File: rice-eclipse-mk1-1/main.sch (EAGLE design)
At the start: 199 parts, among them IC1 LMV321LICTRT, IC10 MCP6N11R, IC11 MCP6N11R, IC12 MCP6N11R, IC13 LMV321LICTRT, IC14 LMV321LICTRT, IC15 LMV321LICTRT, IC16 LMV321LICTRT, IC17 LMV321LICTRT, IC2 LMV321LICTRT, IC3 LMV321LICTRT, IC4 LMV321LICTRT, IC5 MCP6N11R, IC6 LMV321LICTRT, IC7 LMV321LICTRT, IC8 LMV321LICTRT, IC9 LMV321LICTRT, U6 1101M2S3CQE2

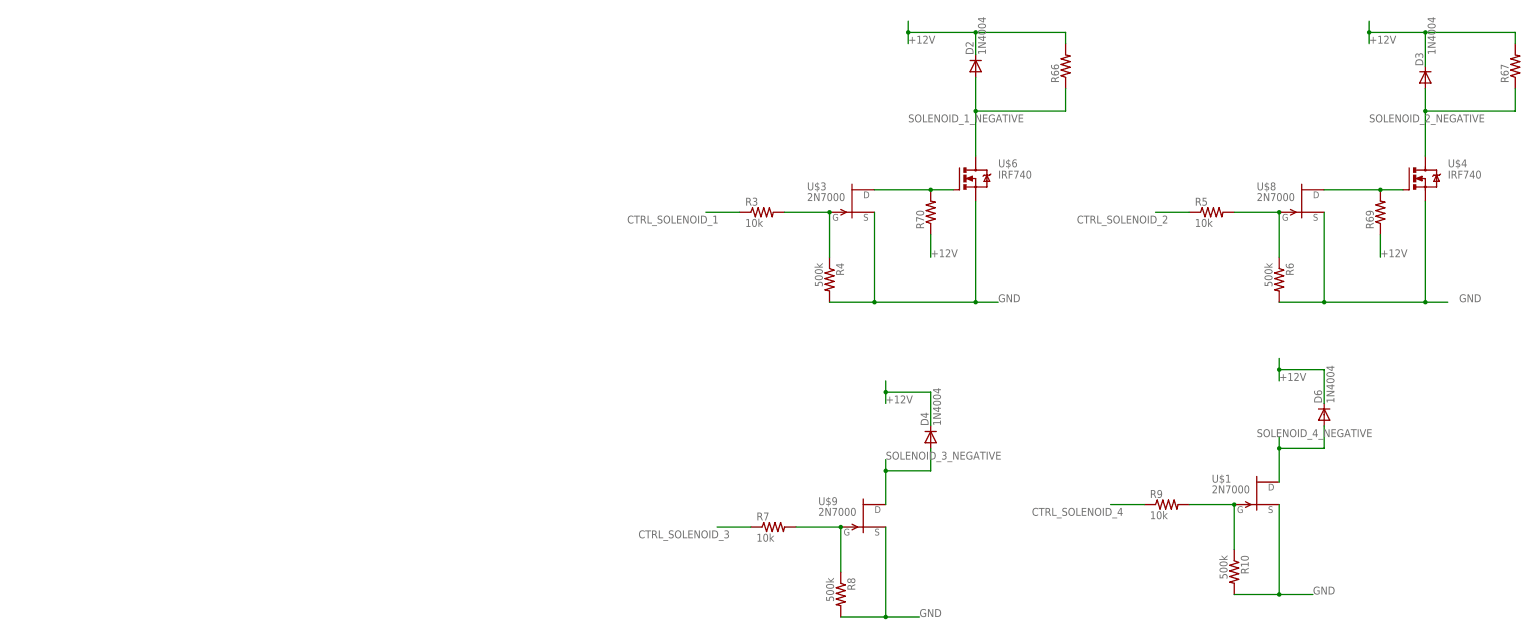
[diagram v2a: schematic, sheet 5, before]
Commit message: Add mosfet driver circuit
Currently have a version with a switch for using either
the 2N7000 or IRF740 (high current). Might be useful to
have a high current option for all the outputs since
propulsion seems to like adding more high-current valves.
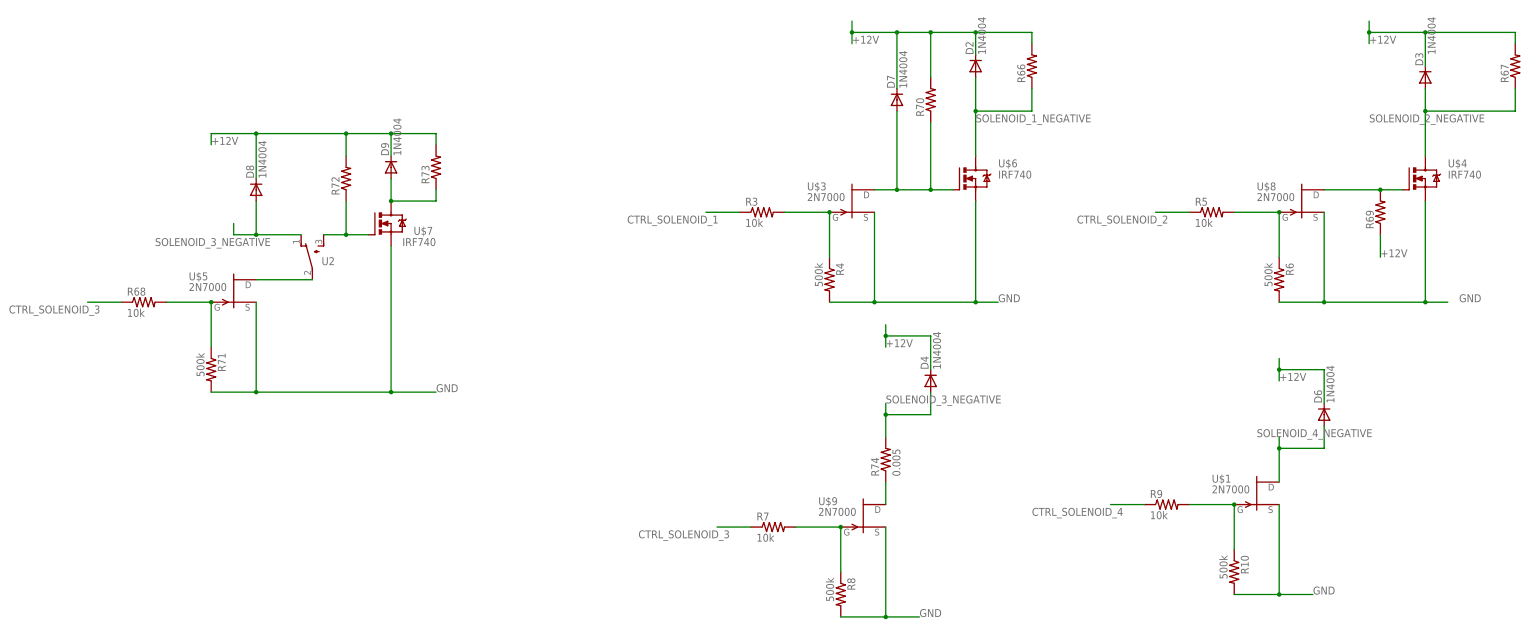
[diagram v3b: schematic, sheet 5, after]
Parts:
- added D7, D8, D9: 1N4004, diode:1N4004
- added R68: 10k, rcl:R-US_R0805
- added R71: 500k, rcl:R-US_R0805
- added R72, R73: (no value), rcl:R-US_R0805
- added R74: 0.005, rcl:R-US_R0805
- added U$5: 2N7000, transistor-fet-extra:2N7000
- added U$7: IRF740, transistor-power:IRF740
- added U2: 1101M2S3CQE2, SLIDE_SW:1101M2S3CQE2
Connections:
- new net N$62: R68.2, R71.1, U$5.G
- new net N$64: U$5.D, U2.P
- new net N$65: R72.1, U$7.G, U2.S
- new net N$66: D9.A, R73.1, U$7.D
- new net N$67: R74.1, U$9.D
- net +12V: now also D7.C, D8.C, D9.C, R70.2, R72.2, R73.2; no longer R70.1
- net CTRL_SOLENOID_3: now also R68.1
- net GND: now also R71.2, U$5.S, U$7.S
- net N$61: now also D7.A, R70.1; no longer R70.2
- net SOLENOID_3_NEGATIVE: now also D8.A, R74.2, U2.O; no longer U$9.D
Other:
- moved on the sheet: D4, R66, R70

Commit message: Add current and voltage sense circuitry
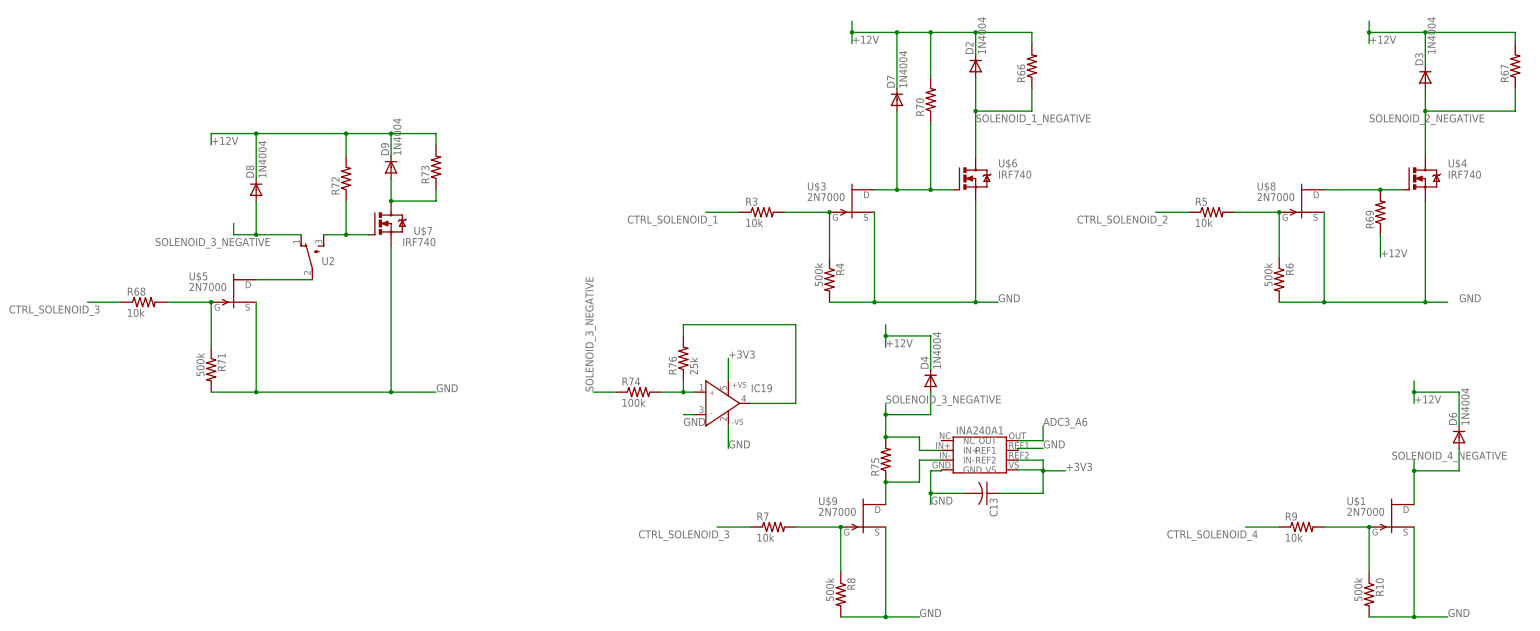
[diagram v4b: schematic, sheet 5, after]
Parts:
- added C13: (no value), rcl:C-USC0805
- added IC18, IC19: LMV321LICTRT, st-microelectronics-extra:LMV321LICTRT
- added R75: (no value), rcl:R-US_R0603
- added R76: 25k, rcl:R-US_R0805
- added U$10: INA240A1, INA240A1:INA240A1
- R74: value 0.005 -> 100k
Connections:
- new net N$68: IC19.IN+, R74.2, R76.1
- new net N$69: IC19.OUT, R76.2
- net +3V3: now also C13.1, IC19.+VS, U$10.REF2, U$10.VS
- net ADC3_A6: now also U$10.OUT
- net GND: now also C13.2, IC19.-VS, IC19.IN-, U$10.GND, U$10.REF1
- net N$67: now also R75.1, U$10.IN-; no longer R74.1
- net SOLENOID_3_NEGATIVE: now also R74.1, R75.2, U$10.IN+; no longer R74.2
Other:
- moved on the sheet: D6, R10, R74, R9, U$1
